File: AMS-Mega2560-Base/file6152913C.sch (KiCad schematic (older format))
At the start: 12 parts

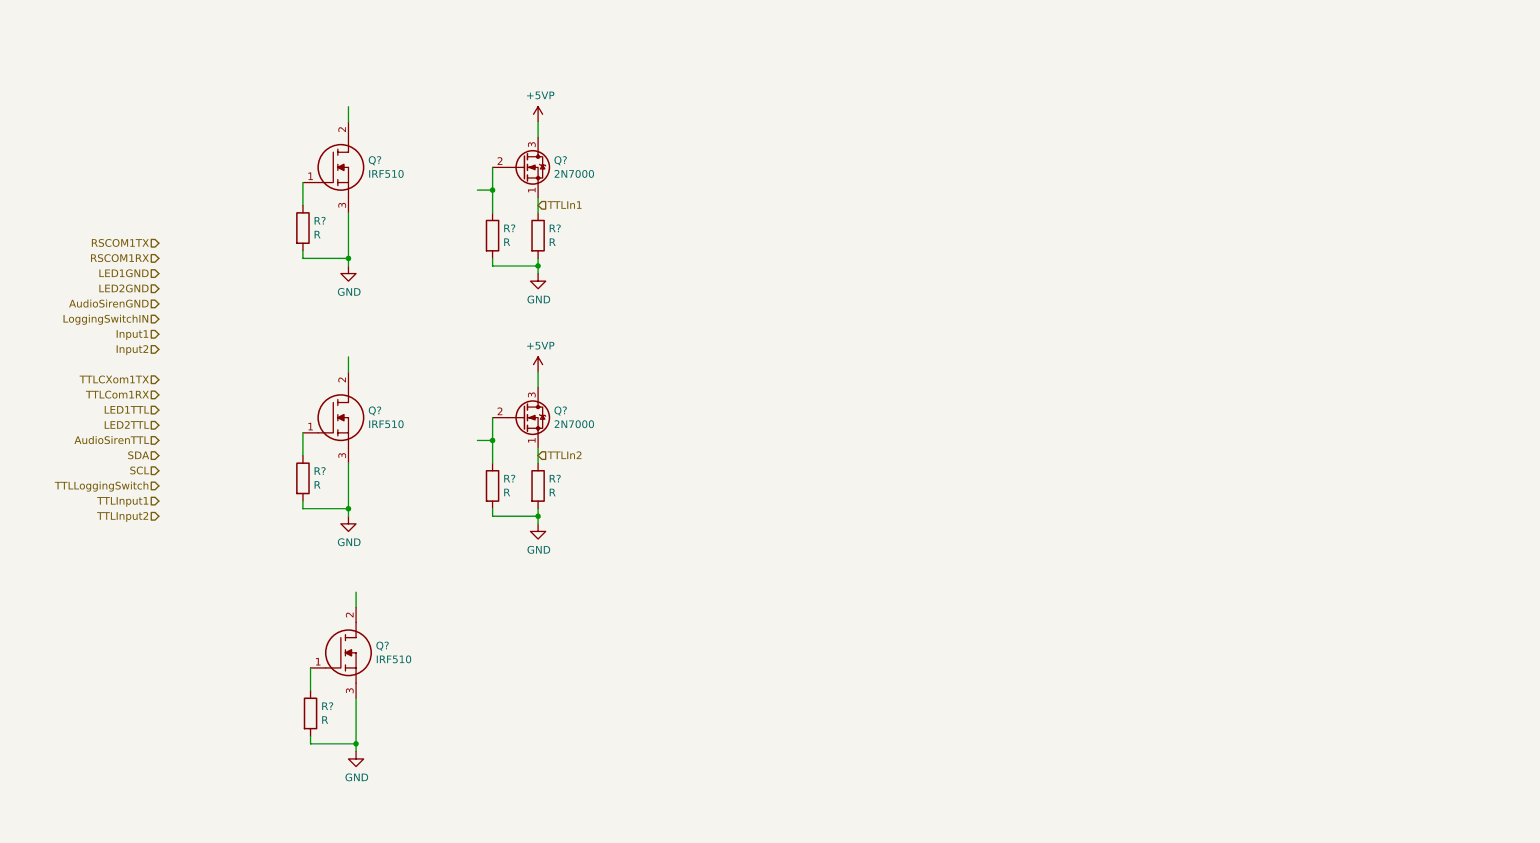
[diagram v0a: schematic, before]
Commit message: still fixing the schematic the coms/RTC need to assign footprints and double check all the parts in that file.
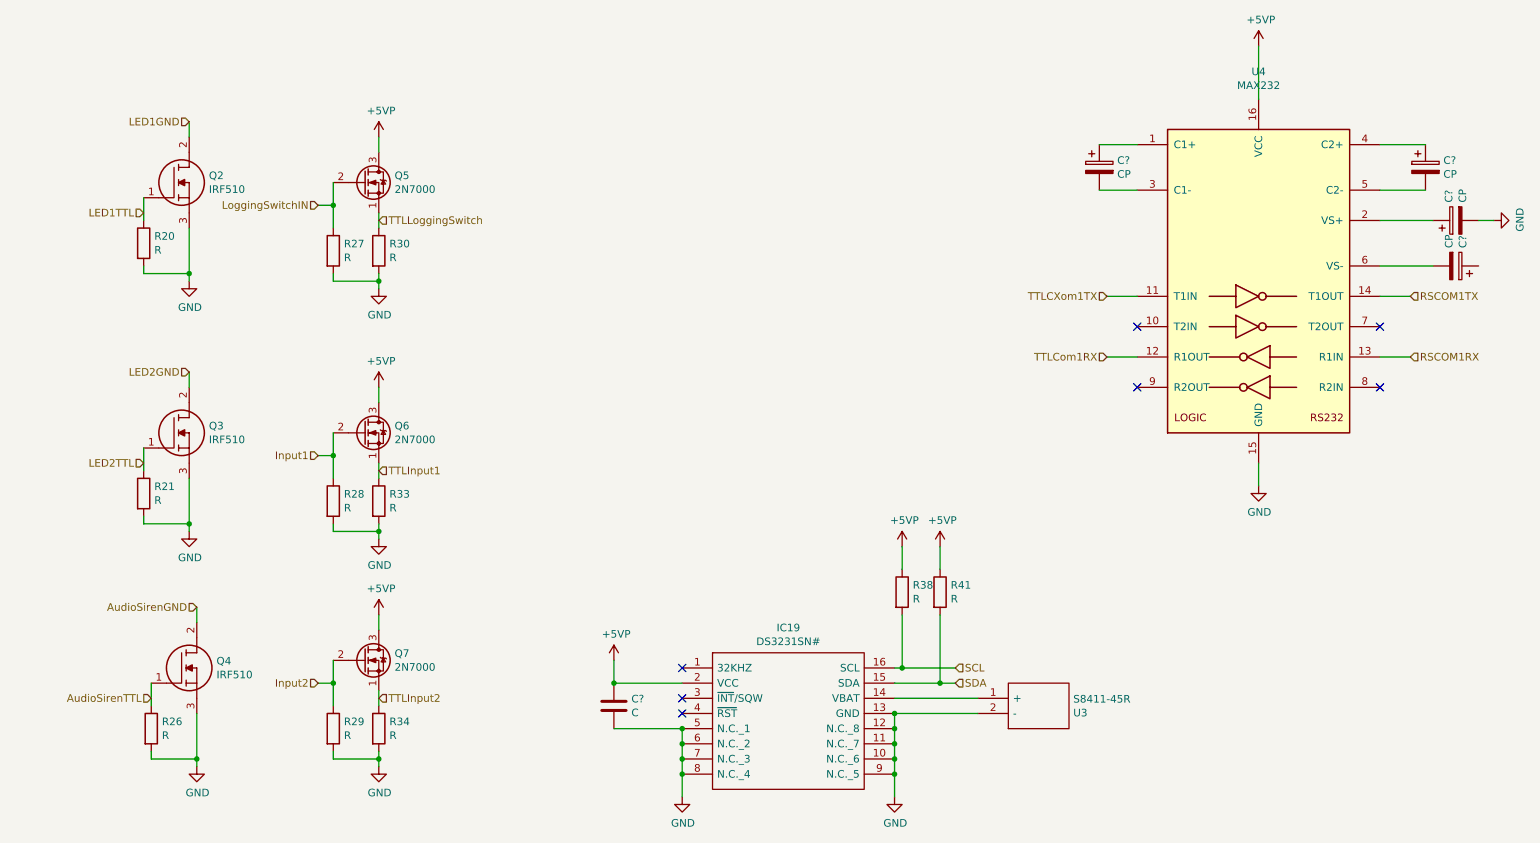
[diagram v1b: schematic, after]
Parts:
- added C?: C, symbol Device:C
- added C? (x4): CP, symbol Device:CP
- added IC19: DS3231SN#, SOIC127P1032X265-16N, symbol SamacSys_Parts:DS3231SN#
- added Q7: 2N7000, Package_TO_SOT_THT:TO-92_Inline, symbol Transistor_FET:2N7000
- added R29, R34, R38, R41: R, Resistor_THT:R_Axial_DIN0207_L6.3mm_D2.5mm_P5.08mm_Vertical, symbol Device:R
- added U3: S8411-45R, S8411-45R_1, symbol SamacSys_Parts:S8411-45R
- added U4: MAX232, symbol Interface_UART:MAX232
- gave numbers to parts that had none: 12
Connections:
- net labels removed: TTLIn1, TTLIn2
- wire segments 36 -> 80
- no-connect marks 0 -> 7
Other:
- moved on the sheet: Q2, Q3, Q4, Q5, Q6, R20, R21, R26, R27, R28, R30, R33

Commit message: fixed the schematics for the RTC, IO and COMs. Realigned the RTD to screw term. need to finish the 3.3v portion of the power systems.
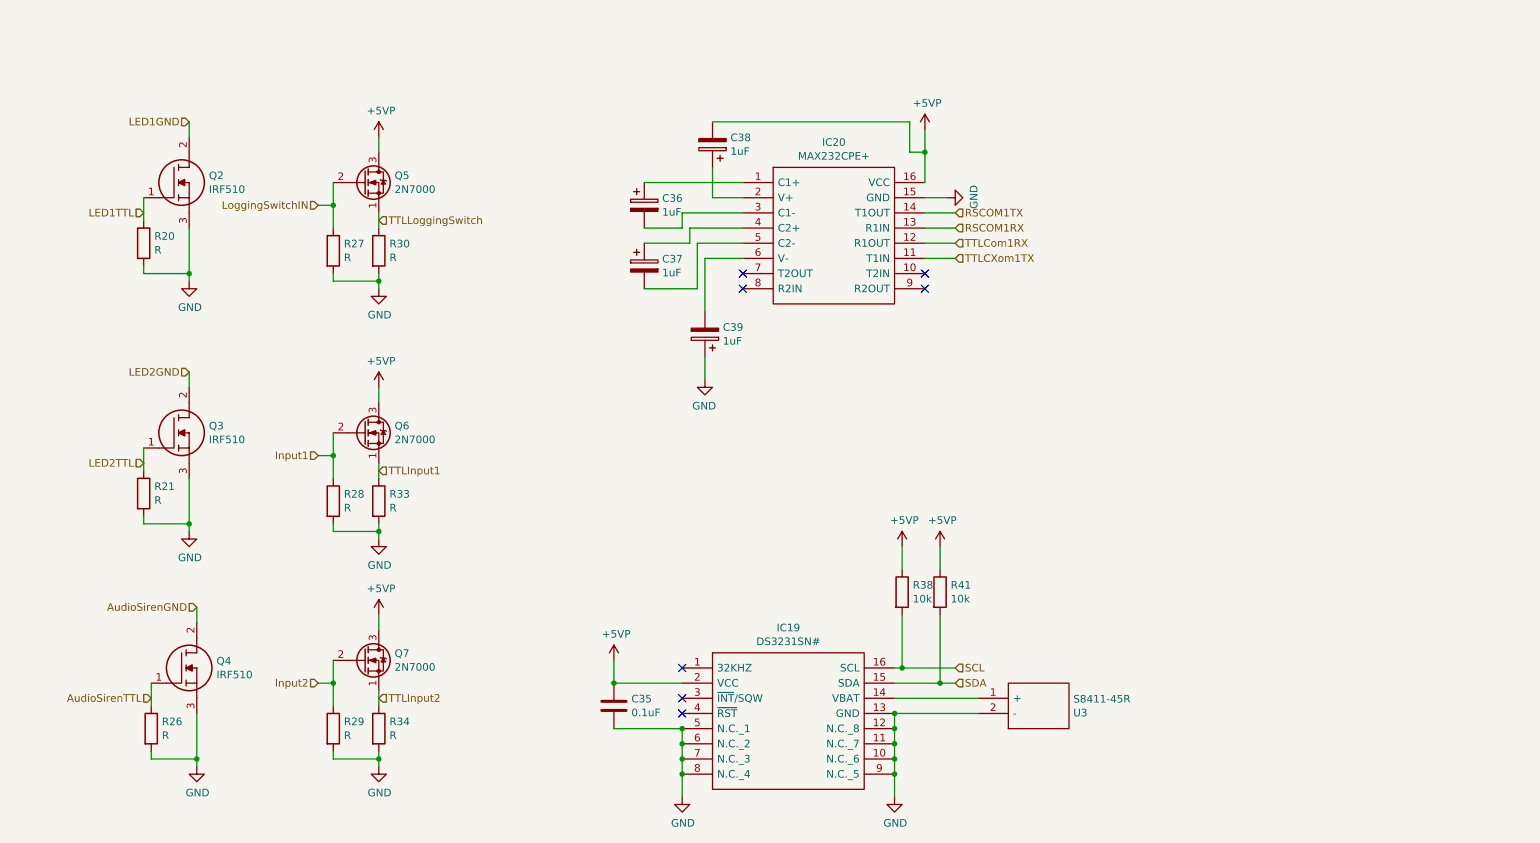
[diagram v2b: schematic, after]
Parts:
- removed U4: MAX232, symbol Interface_UART:MAX232
- added IC20: MAX232CPE+, DIP762W56P254L1918H457Q16N, symbol SamacSys_Parts:MAX232CPE+
- C35: renamed from C?; value C -> 0.1uF; footprint (none) -> Capacitor_THT:C_Rect_L9.0mm_W3.6mm_P7.50mm_MKT
- C36, C37, C38, C39: renamed from C?; value CP -> 1uF; footprint (none) -> Capacitor_THT:CP_Radial_D5.0mm_P2.50mm
- R38, R41: value R -> 10k
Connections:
- net +5VP: now also C38.2, IC20.16 (VCC)
- net GND: now also C39.1, IC20.15 (GND); no longer C38.2
- net RSCOM1RX: now also IC20.13 (R1IN)
- net RSCOM1TX: now also IC20.14 (T1OUT)
- net TTLCXom1TX: now also IC20.11 (T1IN)
- net TTLCom1RX: now also IC20.12 (R1OUT)
- net at C36.1: now also IC20.1 (C1+)
- net at C38.1: now also IC20.2 (V+)
- net at C36.2: now also IC20.3 (C1-)
- net at C37.1: now also IC20.4 (C2+)
- net at C37.2: now also IC20.5 (C2-)
- net at C39.2: now also IC20.6 (V-)
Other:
- moved on the sheet: C36, C37, C38, C39
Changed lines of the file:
@@
 Comment4 ""
 $EndDescr
-Text HLabel 9800 2600 2    50   Input ~ 0
+Text HLabel 6800 2050 2    50   Input ~ 0
 RSCOM1TX
-Text HLabel 9800 3000 2    50   Input ~ 0
+Text HLabel 6800 2150 2    50   Input ~ 0
 RSCOM1RX
 Text HLabel 1750 1450 0    50   Input ~ 0
@@
 Text HLabel 1800 4650 0    50   Input ~ 0
 AudioSirenGND
-Text HLabel 7800 2600 0    50   Input ~ 0
+Text HLabel 6800 2350 2    50   Input ~ 0
 TTLCXom1TX
-Text HLabel 7800 3000 0    50   Input ~ 0
+Text HLabel 6800 2250 2    50   Input ~ 0
 TTLCom1RX
 Text HLabel 1450 2050 0    50   Input ~ 0
@@
 	1    0    0    -1
 $EndComp
-$Comp
-L Interface_UART:MAX232 U4
-U 1 1 61590030
-P 8800 2500
-F 0 "U4" H 8800 3881 50  0000 C CNN
-F 1 "MAX232" H 8800 3790 50  0000 C CNN
-F 2 "" H 8850 1450 50  0001 L CNN
-F 3 "http://www.ti.com/lit/ds/symlink/max232.pdf" H 8800 2600 50  0001 C CNN
-	1    8800 2500
-	1    0    0    -1
-$EndComp
-Wire Wire Line
-	8000 3000 7800 3000
-Wire Wire Line
-	7800 2600 8000 2600
-Wire Wire Line
-	9600 3000 9800 3000
-Wire Wire Line
-	9800 2600 9600 2600
+Wire Wire Line
+	6600 2250 6800 2250
+Wire Wire Line
+	6800 2350 6600 2350
+Wire Wire Line
+	6600 2150 6800 2150
+Wire Wire Line
+	6800 2050 6600 2050
 Wire Wire Line
 	6800 5150 6700 5150
@@
 AR Path="/6152913D/615A086B" Ref="R38"  Part="1"
 F 0 "R38" H 6520 4596 50  0000 L CNN
-F 1 "R" H 6520 4505 50  0000 L CNN
+F 1 "10k" H 6520 4505 50  0000 L CNN
 F 2 "Resistor_THT:R_Axial_DIN0207_L6.3mm_D2.5mm_P5.08mm_Vertical" V 6380 4550 50  0001 C CNN
 F 3 "~" H 6450 4550 50  0001 C CNN
@@
 AR Path="/6152913D/615A16FB" Ref="R41"  Part="1"
 F 0 "R41" H 6770 4596 50  0000 L CNN
-F 1 "R" H 6770 4505 50  0000 L CNN
+F 1 "10k" H 6770 4505 50  0000 L CNN
 F 2 "Resistor_THT:R_Axial_DIN0207_L6.3mm_D2.5mm_P5.08mm_Vertical" V 6630 4550 50  0001 C CNN
 F 3 "~" H 6700 4550 50  0001 C CNN
@@
 L power:+5VP #PWR?
 U 1 1 615AADD5
-P 8800 950
+P 6600 1500
 AR Path="/61493C0E/615AADD5" Ref="#PWR?"  Part="1"
 AR Path="/6153A790/615AADD5" Ref="#PWR?"  Part="1"
 AR Path="/623D3962/615AADD5" Ref="#PWR?"  Part="1"
 AR Path="/6152913D/615AADD5" Ref="#PWR0107"  Part="1"
-F 0 "#PWR0107" H 8800 800 50  0001 C CNN
-F 1 "+5VP" H 8815 1123 50  0000 C CNN
-F 2 "" H 8800 950 50  0001 C CNN
-F 3 "" H 8800 950 50  0001 C CNN
-	1    8800 950
-	1    0    0    -1
-$EndComp
-Wire Wire Line
-	8800 1300 8800 950
+F 0 "#PWR0107" H 6600 1350 50  0001 C CNN
+F 1 "+5VP" H 6615 1673 50  0000 C CNN
+F 2 "" H 6600 1500 50  0001 C CNN
+F 3 "" H 6600 1500 50  0001 C CNN
+	1    6600 1500
+	1    0    0    -1
+$EndComp
+Wire Wire Line
+	6600 1850 6600 1650
 $Comp
 L power:GND #PWR?
@@
 L power:GND #PWR?
 U 1 1 615AF9EF
-P 8800 3850
+P 6750 1950
 AR Path="/6153A790/615AF9EF" Ref="#PWR?"  Part="1"
 AR Path="/623D3962/615AF9EF" Ref="#PWR?"  Part="1"
 AR Path="/6152913D/615AF9EF" Ref="#PWR0108"  Part="1"
-F 0 "#PWR0108" H 8800 3600 50  0001 C CNN
-F 1 "GND" H 8805 3677 50  0000 C CNN
-F 2 "" H 8800 3850 50  0001 C CNN
-F 3 "" H 8800 3850 50  0001 C CNN
-	1    8800 3850
-	1    0    0    -1
-$EndComp
-Wire Wire Line
-	8800 3850 8800 3700
+F 0 "#PWR0108" H 6750 1700 50  0001 C CNN
+F 1 "GND" H 6755 1777 50  0000 C CNN
+F 2 "" H 6750 1950 50  0001 C CNN
+F 3 "" H 6750 1950 50  0001 C CNN
+	1    6750 1950
+	0    -1   -1   0
+$EndComp
+Wire Wire Line
+	6750 1950 6600 1950
 Wire Wire Line
 	5000 5900 5000 5750
@@
 AR Path="/6153A790/615C48D3" Ref="#PWR?"  Part="1"
 AR Path="/623D3962/615C48D3" Ref="#PWR?"  Part="1"
-AR Path="/6152913D/615C48D3" Ref="#PWR?"  Part="1"
-F 0 "#PWR?" H 4550 4850 50  0001 C CNN
+AR Path="/6152913D/615C48D3" Ref="#PWR0109"  Part="1"
+F 0 "#PWR0109" H 4550 4850 50  0001 C CNN
 F 1 "+5VP" H 4565 5173 50  0000 C CNN
 F 2 "" H 4550 5000 50  0001 C CNN
@@
 $EndComp
 $Comp
-L Device:C C?
+L Device:C C35
 U 1 1 615C60E1
 P 4550 5300
-F 0 "C?" H 4665 5346 50  0000 L CNN
-F 1 "C" H 4665 5255 50  0000 L CNN
-F 2 "" H 4588 5150 50  0001 C CNN
+F 0 "C35" H 4665 5346 50  0000 L CNN
+F 1 "0.1uF" H 4665 5255 50  0000 L CNN
+F 2 "Capacitor_THT:C_Rect_L9.0mm_W3.6mm_P7.50mm_MKT" H 4588 5150 50  0001 C CNN
 F 3 "~" H 4550 5300 50  0001 C CNN
 	1    4550 5300
@@
 NoConn ~ 5000 5250
 NoConn ~ 5000 5350
-NoConn ~ 8000 3200
-NoConn ~ 8000 2800
-NoConn ~ 9600 3200
-NoConn ~ 9600 2800
-$Comp
-L Device:CP C?
+$Comp
+L Device:CP C36
 U 1 1 615DA0D3
-P 7750 1750
-F 0 "C?" H 7868 1796 50  0000 L CNN
-F 1 "CP" H 7868 1705 50  0000 L CNN
-F 2 "" H 7788 1600 50  0001 C CNN
-F 3 "~" H 7750 1750 50  0001 C CNN
-	1    7750 1750
-	1    0    0    -1
-$EndComp
-$Comp
-L Device:CP C?
+P 4750 2000
+F 0 "C36" H 4868 2046 50  0000 L CNN
+F 1 "1uF" H 4868 1955 50  0000 L CNN
+F 2 "Capacitor_THT:CP_Radial_D5.0mm_P2.50mm" H 4788 1850 50  0001 C CNN
+F 3 "~" H 4750 2000 50  0001 C CNN
+	1    4750 2000
+	1    0    0    -1
+$EndComp
+$Comp
+L Device:CP C37
 U 1 1 615DB4D6
-P 9900 1750
-F 0 "C?" H 10018 1796 50  0000 L CNN
-F 1 "CP" H 10018 1705 50  0000 L CNN
-F 2 "" H 9938 1600 50  0001 C CNN
-F 3 "~" H 9900 1750 50  0001 C CNN
-	1    9900 1750
-	1    0    0    -1
-$EndComp
-$Comp
-L Device:CP C?
+P 4750 2400
+F 0 "C37" H 4868 2446 50  0000 L CNN
+F 1 "1uF" H 4868 2355 50  0000 L CNN
+F 2 "Capacitor_THT:CP_Radial_D5.0mm_P2.50mm" H 4788 2250 50  0001 C CNN
+F 3 "~" H 4750 2400 50  0001 C CNN
+	1    4750 2400
+	1    0    0    -1
+$EndComp
+$Comp
+L Device:CP C38
 U 1 1 615DD20F
-P 10100 2100
-F 0 "C?" H 10218 2146 50  0000 L CNN
-F 1 "CP" H 10218 2055 50  0000 L CNN
-F 2 "" H 10138 1950 50  0001 C CNN
-F 3 "~" H 10100 2100 50  0001 C CNN
-	1    10100 2100
-	0    -1   -1   0
-$EndComp
-$Comp
-L Device:CP C?
+P 5200 1600
+F 0 "C38" H 5082 1554 50  0000 R CNN
+F 1 "1uF" H 5082 1645 50  0000 R CNN
+F 2 "Capacitor_THT:CP_Radial_D5.0mm_P2.50mm" H 5238 1450 50  0001 C CNN
+F 3 "~" H 5200 1600 50  0001 C CNN
+	1    5200 1600
+	-1   0    0    1
+$EndComp
+$Comp
+L Device:CP C39
 U 1 1 615E0CC2
-P 10100 2400
-F 0 "C?" H 10218 2446 50  0000 L CNN
-F 1 "CP" H 10218 2355 50  0000 L CNN
-F 2 "" H 10138 2250 50  0001 C CNN
-F 3 "~" H 10100 2400 50  0001 C CNN
-	1    10100 2400
-	0    1    -1   0
-$EndComp
-Wire Wire Line
-	8000 1900 7750 1900
-Wire Wire Line
-	7750 1600 8000 1600
-Wire Wire Line
-	9600 1900 9900 1900
-Wire Wire Line
-	9900 1600 9600 1600
-Wire Wire Line
-	9950 2100 9600 2100
-Wire Wire Line
-	9950 2400 9600 2400
-$Comp
-L power:GND #PWR?
-U 1 1 615EFFBB
-P 10350 2100
-AR Path="/6153A790/615EFFBB" Ref="#PWR?"  Part="1"
-AR Path="/623D3962/615EFFBB" Ref="#PWR?"  Part="1"
-AR Path="/6152913D/615EFFBB" Ref="#PWR?"  Part="1"
-F 0 "#PWR?" H 10350 1850 50  0001 C CNN
-F 1 "GND" H 10355 1927 50  0000 C CNN
-F 2 "" H 10350 2100 50  0001 C CNN
-F 3 "" H 10350 2100 50  0001 C CNN
-	1    10350 2100
-	0    -1   -1   0
-$EndComp
-Wire Wire Line
-	10250 2100 10350 2100
+P 5150 2850
+F 0 "C39" H 5032 2804 50  0000 R CNN
+F 1 "1uF" H 5032 2895 50  0000 R CNN
+F 2 "Capacitor_THT:CP_Radial_D5.0mm_P2.50mm" H 5188 2700 50  0001 C CNN
+F 3 "~" H 5150 2850 50  0001 C CNN
+	1    5150 2850
+	-1   0    0    1
+$EndComp
+Wire Wire Line
+	5000 2150 4750 2150
+Wire Wire Line
+	5150 2700 5150 2350
+$Comp
+L power:GND #PWR?
+U 1 1 61600BAF
+P 5150 3150
+AR Path="/6153A790/61600BAF" Ref="#PWR?"  Part="1"
+AR Path="/623D3962/61600BAF" Ref="#PWR?"  Part="1"
+AR Path="/6152913D/61600BAF" Ref="#PWR0110"  Part="1"
+F 0 "#PWR0110" H 5150 2900 50  0001 C CNN
+F 1 "GND" H 5155 2977 50  0000 C CNN
+F 2 "" H 5150 3150 50  0001 C CNN
+F 3 "" H 5150 3150 50  0001 C CNN
+	1    5150 3150
+	-1   0    0    -1
+$EndComp
+Wire Wire Line
+	5150 3000 5150 3150
+$Comp
+L SamacSys_Parts:MAX232CPE+ IC20
+U 1 1 61604267
+P 5400 1850
+F 0 "IC20" H 6000 2115 50  0000 C CNN
+F 1 "MAX232CPE+" H 6000 2024 50  0000 C CNN
+F 2 "DIP762W56P254L1918H457Q16N" H 6450 1950 50  0001 L CNN
+F 3 "http://datasheets.maximintegrated.com/en/ds/MAX220-MAX249.pdf" H 6450 1850 50  0001 L CNN
+F 4 "TRANSCEIVER MAX 232 CPE MAX232CPE+, Line Transceiver, EIA/TIA-232-E, RS-232, V.24, V.28 2-TX 2-RX 2-TRX, 5 V, 16-Pin PDIP" H 6450 1750 50  0001 L CNN "Description"
+F 5 "4.572" H 6450 1650 50  0001 L CNN "Height"
+F 6 "700-MAX232CPE" H 6450 1550 50  0001 L CNN "Mouser Part Number"
+F 7 "https://www.mouser.co.uk/ProductDetail/Maxim-Integrated/MAX232CPE%2b?qs=1THa7WoU59H6WLBcdj%252BTOQ%3D%3D" H 6450 1450 50  0001 L CNN "Mouser Price/Stock"
+F 8 "Maxim Integrated" H 6450 1350 50  0001 L CNN "Manufacturer_Name"
+F 9 "MAX232CPE+" H 6450 1250 50  0001 L CNN "Manufacturer_Part_Number"
+	1    5400 1850
+	1    0    0    -1
+$EndComp
+Wire Wire Line
+	4750 1850 5400 1850
+Wire Wire Line
+	5000 2150 5000 2050
+Wire Wire Line
+	5000 2050 5400 2050
+Wire Wire Line
+	4750 2250 5050 2250
+Wire Wire Line
+	5050 2250 5050 2150
+Wire Wire Line
+	5050 2150 5400 2150
+Wire Wire Line
+	4750 2550 5100 2550
+Wire Wire Line
+	5100 2550 5100 2250
+Wire Wire Line
+	5100 2250 5400 2250
+Wire Wire Line
+	5400 1950 5200 1950
+Wire Wire Line
+	5200 1950 5200 1750
+Wire Wire Line
+	5200 1450 6500 1450
+Wire Wire Line
+	6500 1450 6500 1650
+Wire Wire Line
+	6500 1650 6600 1650
+Connection ~ 6600 1650
+Wire Wire Line
+	6600 1650 6600 1500
+Wire Wire Line
+	5150 2350 5400 2350
+NoConn ~ 5400 2450
+NoConn ~ 5400 2550
+NoConn ~ 6600 2450
+NoConn ~ 6600 2550
 $EndSCHEMATC

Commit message: rearranging some of the hw design before i rename the repo.
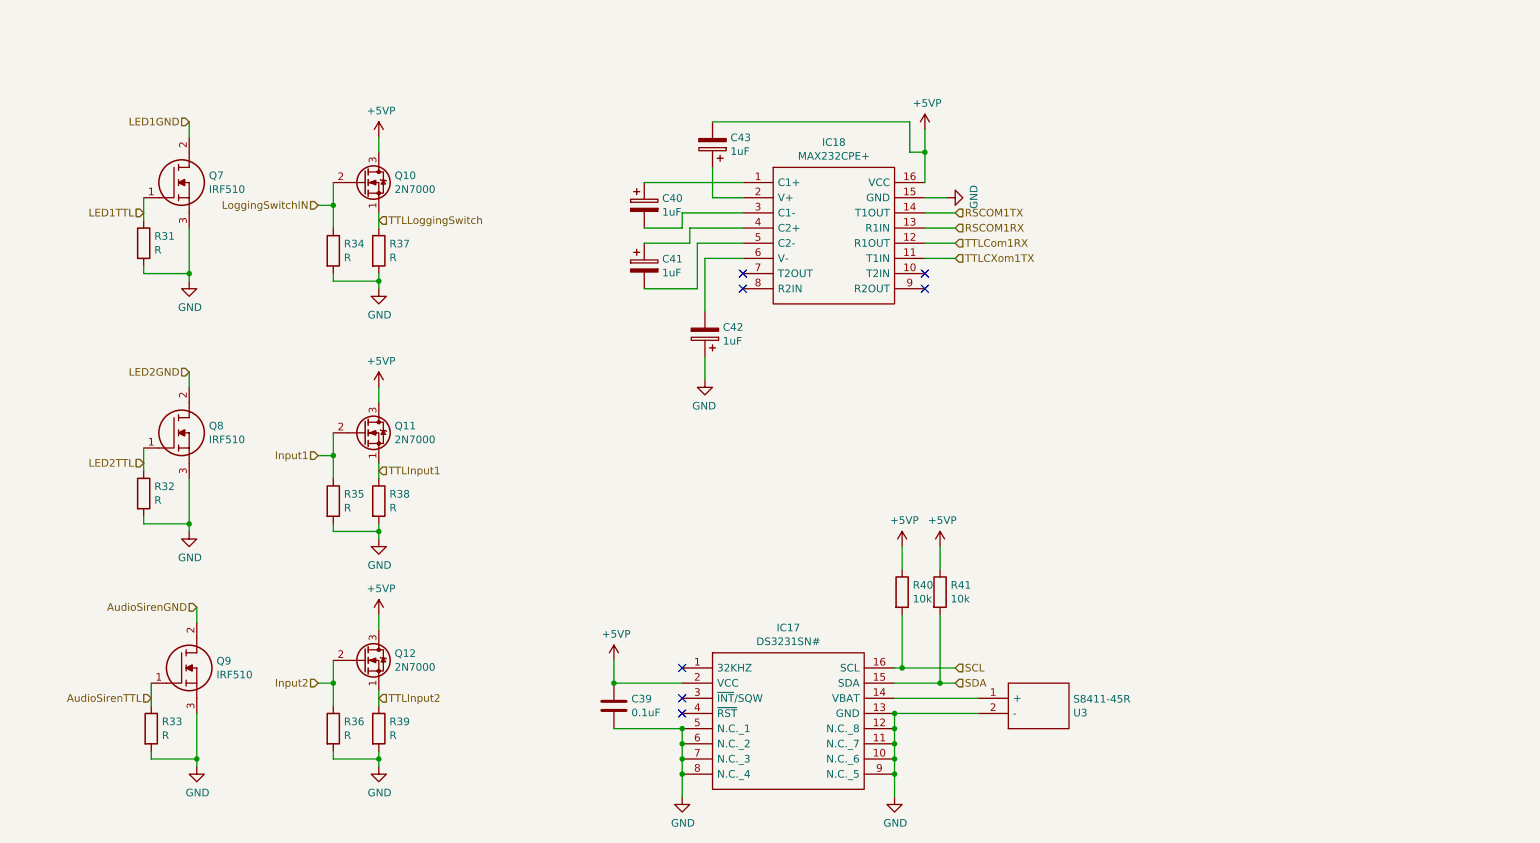
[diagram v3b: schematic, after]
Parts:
- IC17: renamed from IC19; footprint SOIC127P1032X265-16N -> SamacSys_Parts:SOIC127P1032X265-16N
- IC18: renamed from IC20; footprint DIP762W56P254L1918H457Q16N -> SamacSys_Parts:DIP762W56P254L1918H457Q16N
- U3: footprint S8411-45R_1 -> SamacSys_Parts:S8411-45R_1
- renumbered C35 to C39, C36 to C40, C37 to C41, C39 to C42, C38 to C43, Q5 to Q10, Q6 to Q11, Q7 to Q12, Q2 to Q7, Q3 to Q8, Q4 to Q9, R20 to R31, R21 to R32, R26 to R33, R27 to R34, R28 to R35, R29 to R36, R30 to R37, R33 to R38, R34 to R39, R38 to R40
